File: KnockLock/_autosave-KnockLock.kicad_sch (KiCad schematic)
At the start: 49 parts, among them IC1 ESP32-C3-WROOM-02-N4, IC2 LM2575-3.3WT, J1 2477, J2 UJ2-B-HR-G-TH, J3 TBP04R12-500-03BE, J4 UART, J5 Boot Pins, Q1 IRLML6402TRPBF, Q2 BC547B, U1 ADXL345BCCZ-RL7

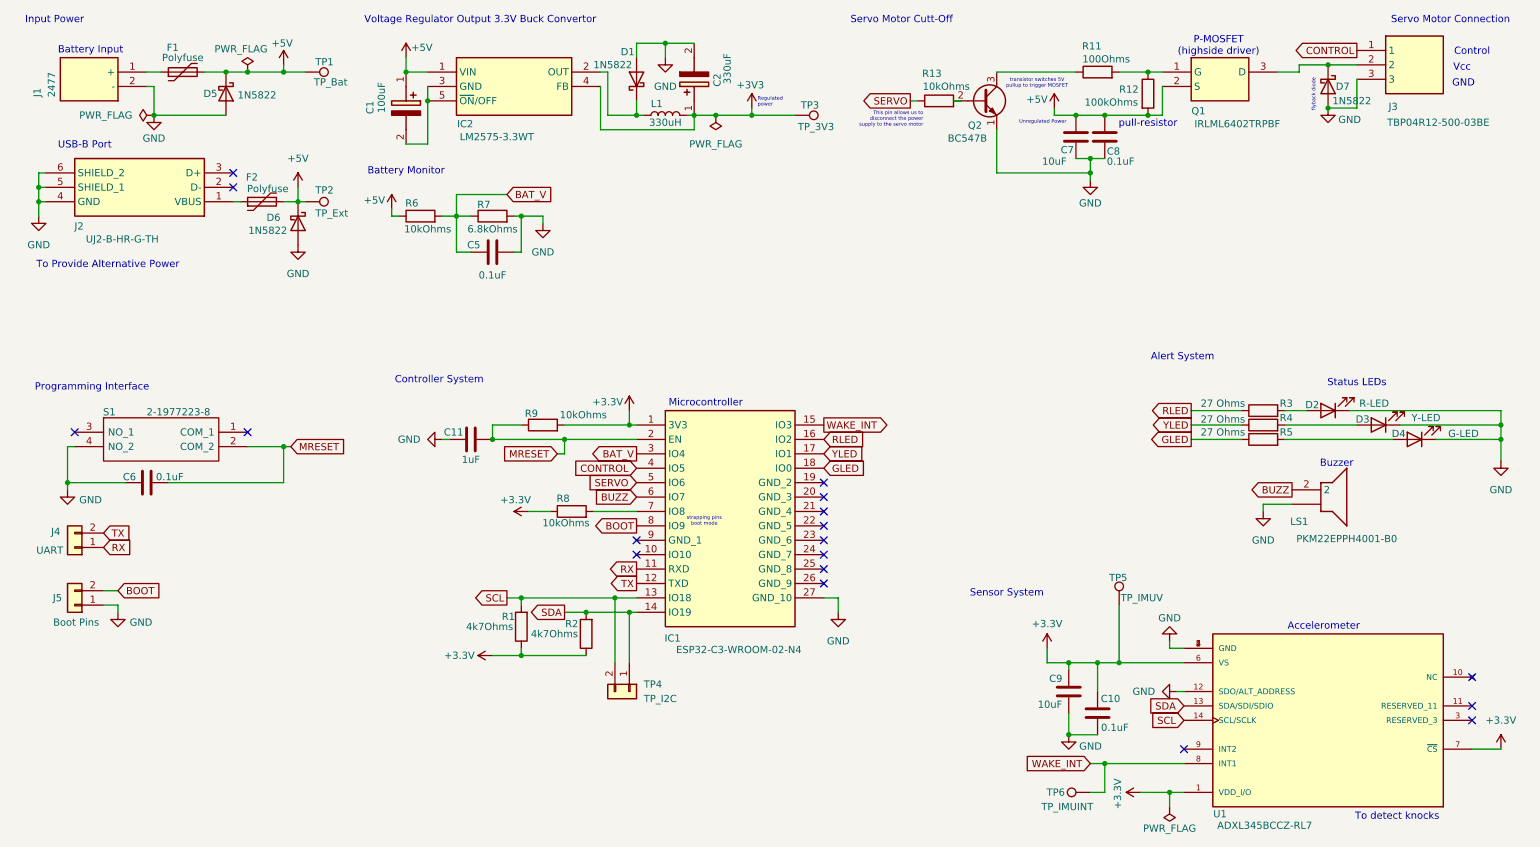
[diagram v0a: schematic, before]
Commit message: Some minor changes - removed 2nd set of decoupling capacitors after voltage regulator, formatting
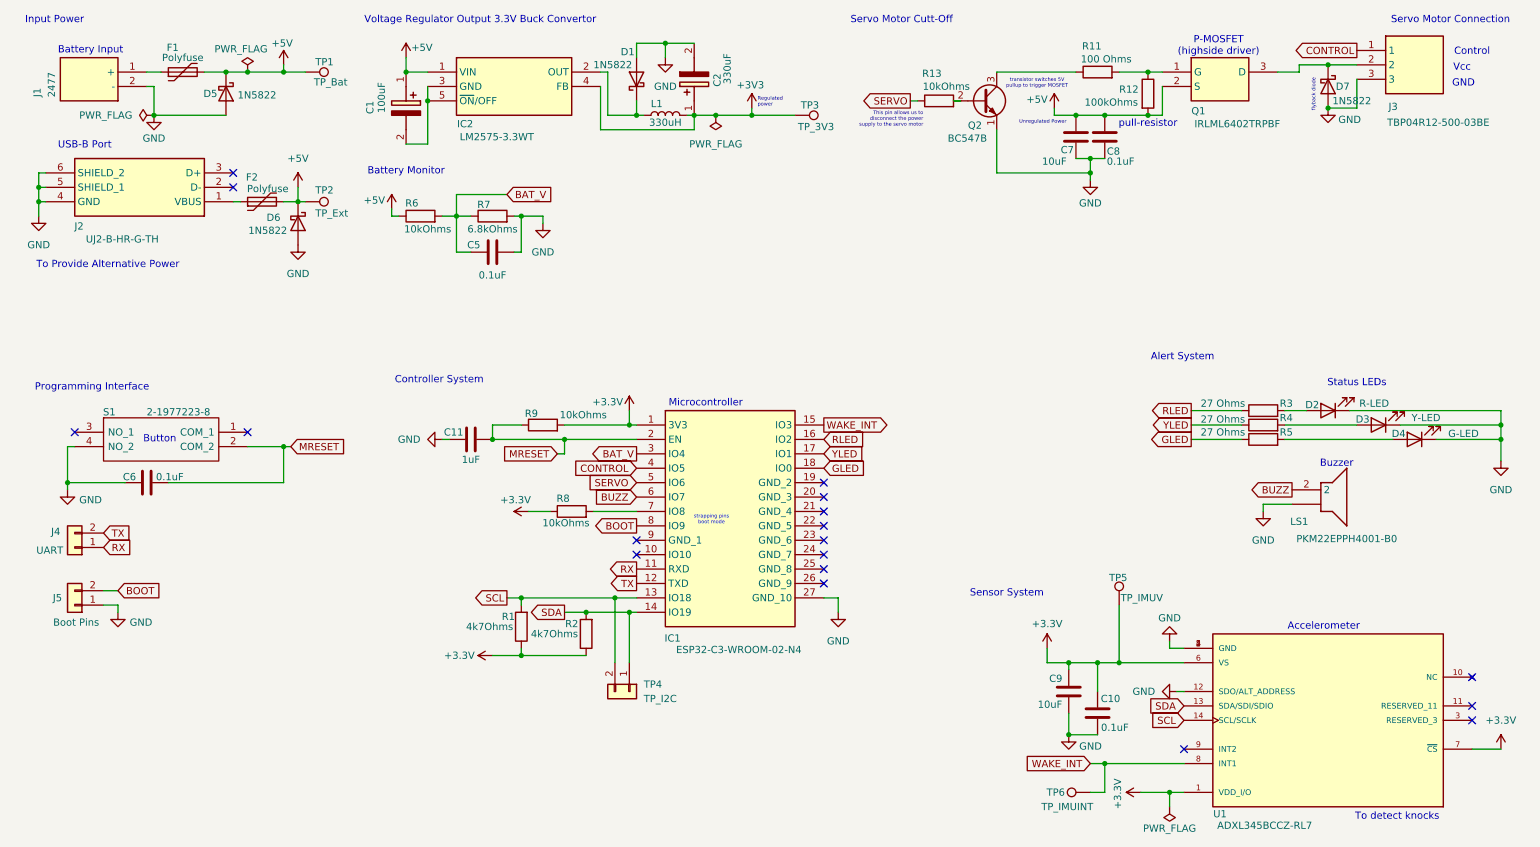
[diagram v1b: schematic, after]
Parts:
- R11: value 100Ohms -> 100 Ohms
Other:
- note added: "Button"
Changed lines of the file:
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@@
 		)
 	)
+	(text "Button"
+		(exclude_from_sim no)
+		(at 41.656 90.17 0)
+		(effects
+			(font
+				(size 1.27 1.27)
+			)
+		)
+	)
 	(text "Programming Interface"
 		(exclude_from_sim no)
@@
 	(text "strapping pins\nboot mode"
 		(exclude_from_sim no)
-		(at 137.668 104.648 0)
+		(at 138.938 104.394 0)
 		(effects
 			(font
@@
 			)
 		)
-		(property "Value" "100Ohms"
+		(property "Value" "100 Ohms"
 			(at 208.534 23.114 90)
 			(effects
